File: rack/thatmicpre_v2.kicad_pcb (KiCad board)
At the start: 2 copper layers, 140 x 74.2 mm, 89 parts, among them J1 CON-SOCJ-2155, J10 Angled pinheader, J2 NC3FBH2, J3 NC3MBH1, J4 Female header, J5 Male pinheader, J6 Female header, J7 Male pinheader, J8 Angled pinheader, J9 NMJ6HFD2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

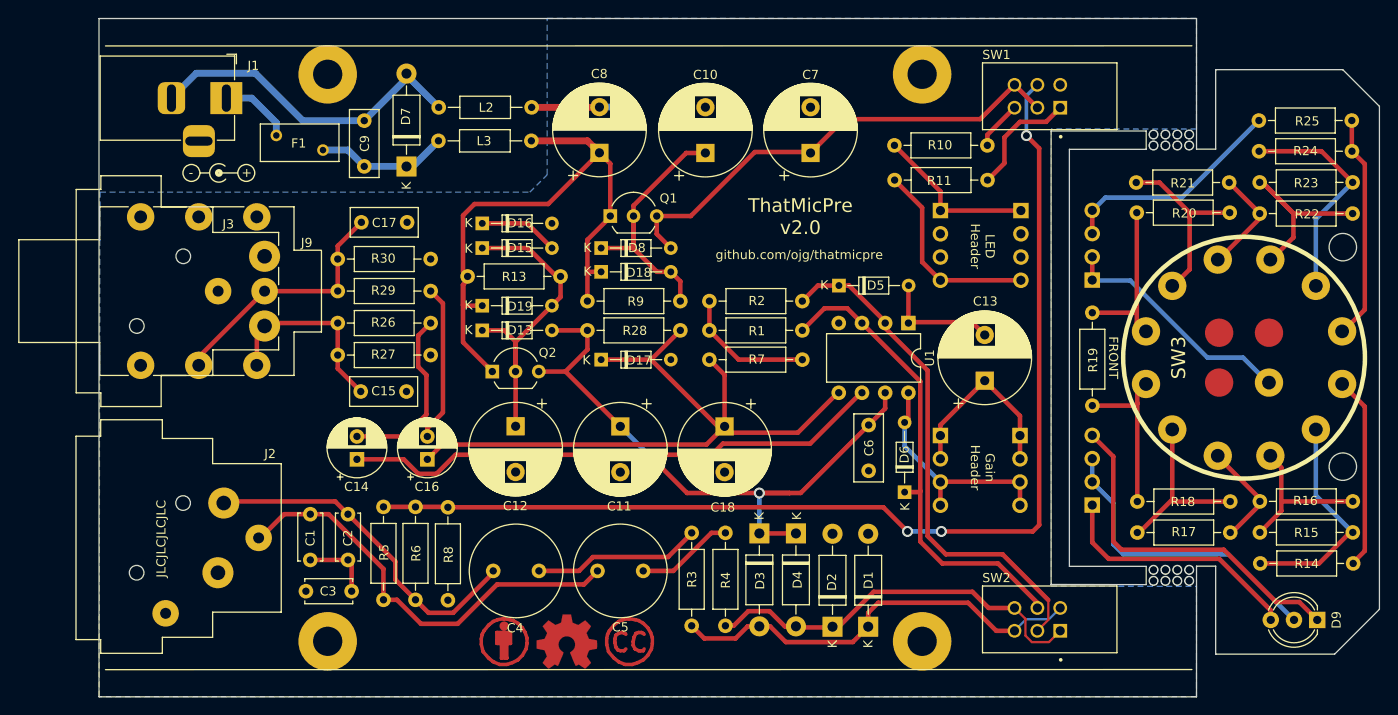
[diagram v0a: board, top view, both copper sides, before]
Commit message: The motherboard width is compatible with the new case
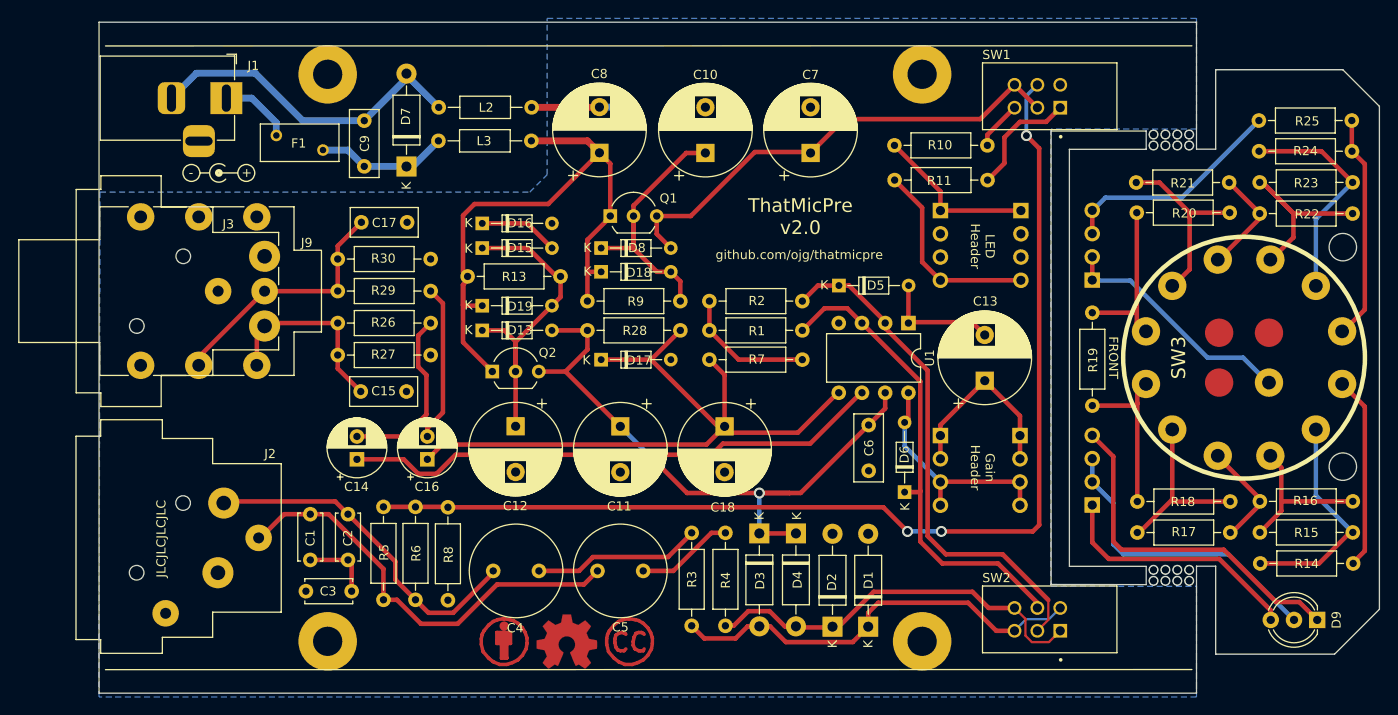
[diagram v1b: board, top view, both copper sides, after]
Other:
- board size 140 x 74.2 mm -> 140 x 73.4 mm
